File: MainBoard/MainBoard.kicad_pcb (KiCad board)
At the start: 2 copper layers, 31.8 x 110 mm, 41 parts, among them U1 TL074CN, U2 TL074CN, U3 TL074CN

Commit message: updated placement
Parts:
- D1: value 1N5934B -> 1N5394B; footprint 1N5934B:P2_DO-201 -> 1N5349B:P2_DO-201
- D2: value 1N5934B -> 1N5349B; footprint 1N5934B:P2_DO-201 -> 1N5349B:P2_DO-201
- moved C2 99.5 mm to (169.3, 144.5), turned to 90 degrees
- moved U1 95.0 mm to (155.3, 149.3)
- moved R3 91.5 mm to (150.5, 138.8)
- moved R1 90.5 mm to (150.5, 135.5), turned to 0 degrees
- moved C1 89.3 mm to (169.4, 152.7), turned to 90 degrees
- moved R9 89.1 mm to (139.6, 148.5), turned to 90 degrees
- moved D2 86.9 mm to (147.5, 49.6), turned to 0 degrees
- moved R2 86.5 mm to (143.3, 138.5), turned to -90 degrees
- moved R4 82.4 mm to (146.5, 125.7), turned to -90 degrees
- moved R16 81.6 mm to (160.6, 142.2), turned to 180 degrees
- moved R10 78.8 mm to (143.2, 135.8), turned to 90 degrees
- moved JP1 77.3 mm to (168.5, 70.9), turned to 90 degrees
- moved D1 77.1 mm to (147.5, 57.8), turned to 180 degrees
- moved F2 74.9 mm to (164.3, 50.5), turned to 0 degrees
- moved F1 73.7 mm to (159.3, 63.2), turned to -90 degrees
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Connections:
- Jheader2 pad 12: Output8 -> Output5
- Jheader2 pad 13: Output9 -> Output8
- Jheader2 pad 14: Output10 -> Output6
- Jheader2 pad 7: Output5 -> Output9
- Jheader2 pad 8: Output6 -> Output10
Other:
- board size 31.8 x 110 mm -> 34.4 x 110 mm

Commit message: first pass at routing mainboard
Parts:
- added R25: 100k, Resistor_THT:R_Axial_DIN0207_L6.3mm_D2.5mm_P10.16mm_Horizontal, F.Cu at (149.5, 141.5)
- Jheader2: footprint 61301611021:61301611021 -> 75168-116-20LF:AMPHENOL_75168-116-20LF
- moved F2 24.1 mm to (169.7, 74.0), turned to 90 degrees
- moved R16 23.2 mm to (146.2, 124.1), turned to 90 degrees
- moved C8 19.1 mm to (153.5, 55.3)
- moved R7 18.7 mm to (139.9, 54.4), turned to 0 degrees
- moved C2 18.3 mm to (151.0, 144.4), turned to -90 degrees
- moved R3 17.0 mm to (140.8, 152.8)
- moved R20 16.5 mm to (169.0, 118.0), turned to 90 degrees
- moved C7 11.2 mm to (165.7, 68.9)
- moved JP1 10.3 mm to (168.6, 60.6)
- moved F1 9.52 mm to (159.8, 53.7), turned to 90 degrees
- moved D1 8.07 mm to (152.8, 63.9)
- moved Jheader2 7.90 mm to (141.8, 91.5)
- moved C1 7.18 mm to (166.3, 146.2)
- moved R12 6.91 mm to (146.2, 100.7)
- moved C5 6.84 mm to (162.5, 85.1), turned to 180 degrees
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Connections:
- Jheader2 pad 10: InputBus4 -> Output10
- Jheader2 pad 11: Output7 -> InputBus4
- Jheader2 pad 12: Output5 -> Output4
- Jheader2 pad 13: Output8 -> Output9
- Jheader2 pad 14: Output6 -> Output12
- Jheader2 pad 15: Output11 -> Output3
- Jheader2 pad 16: Output12 -> Output11
- U1 pad 12: InputBus2 -> Net-(U1-4IN+)
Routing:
- net GND: track 0.00 -> 238.2 mm
- net -v: track 0.00 -> 144.6 mm
- net +v: track 0.00 -> 120.8 mm
- net InputBus2: track 0.00 -> 81.1 mm
- net InputBus3: track 0.00 -> 61.9 mm
- net Output3: track 0.00 -> 52.9 mm
- net Net-(U2-3IN-): track 0.00 -> 48.9 mm
- net Output4: track 0.00 -> 47.1 mm
- net Net-(U1-2IN-): track 0.00 -> 44.5 mm
- net InputBus4: track 0.00 -> 44.4 mm
- net Net-(U2-3IN+): track 0.00 -> 38.7 mm
- net Net-(U3-4IN-): track 0.00 -> 37.5 mm
- net Output2: track 0.00 -> 33.9 mm
- net InputBus1: track 0.00 -> 33.6 mm
- net Net-(U1-3IN-): track 0.00 -> 33.0 mm
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
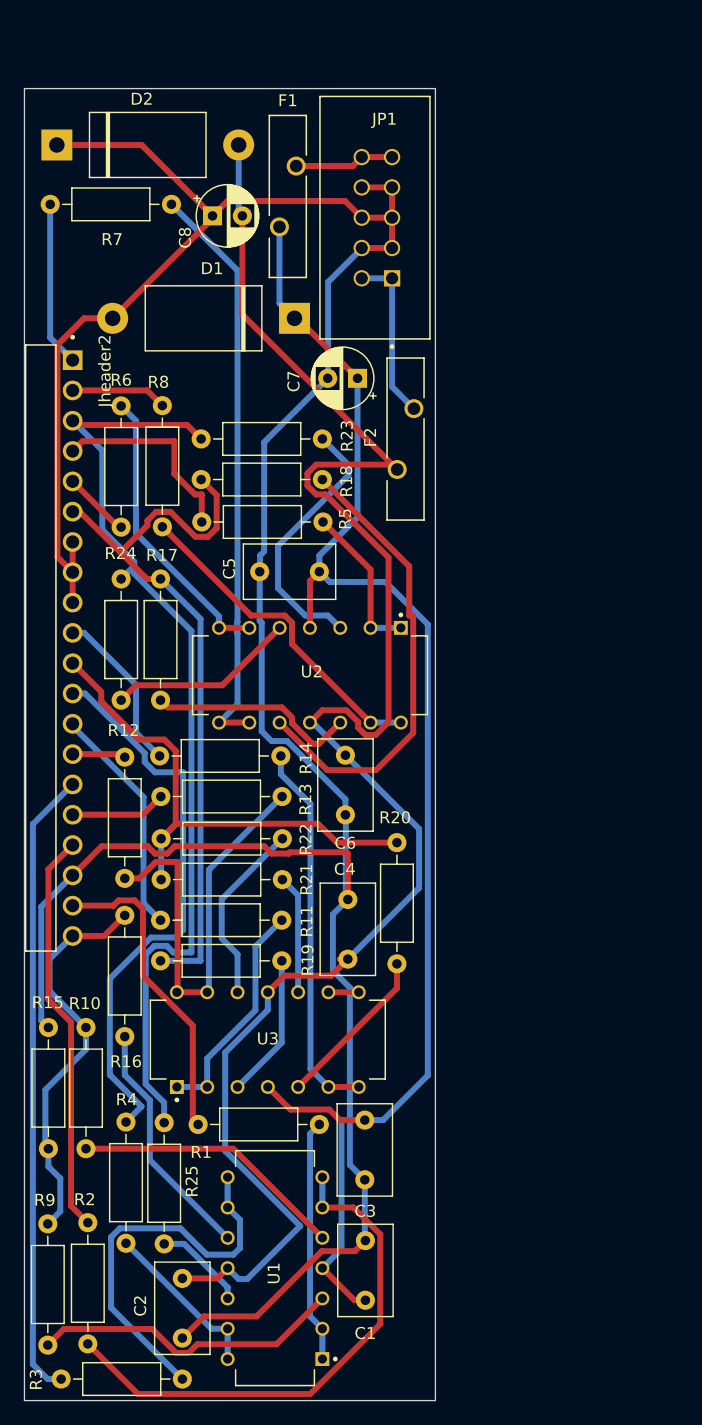
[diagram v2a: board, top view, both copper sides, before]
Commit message: added ground plane
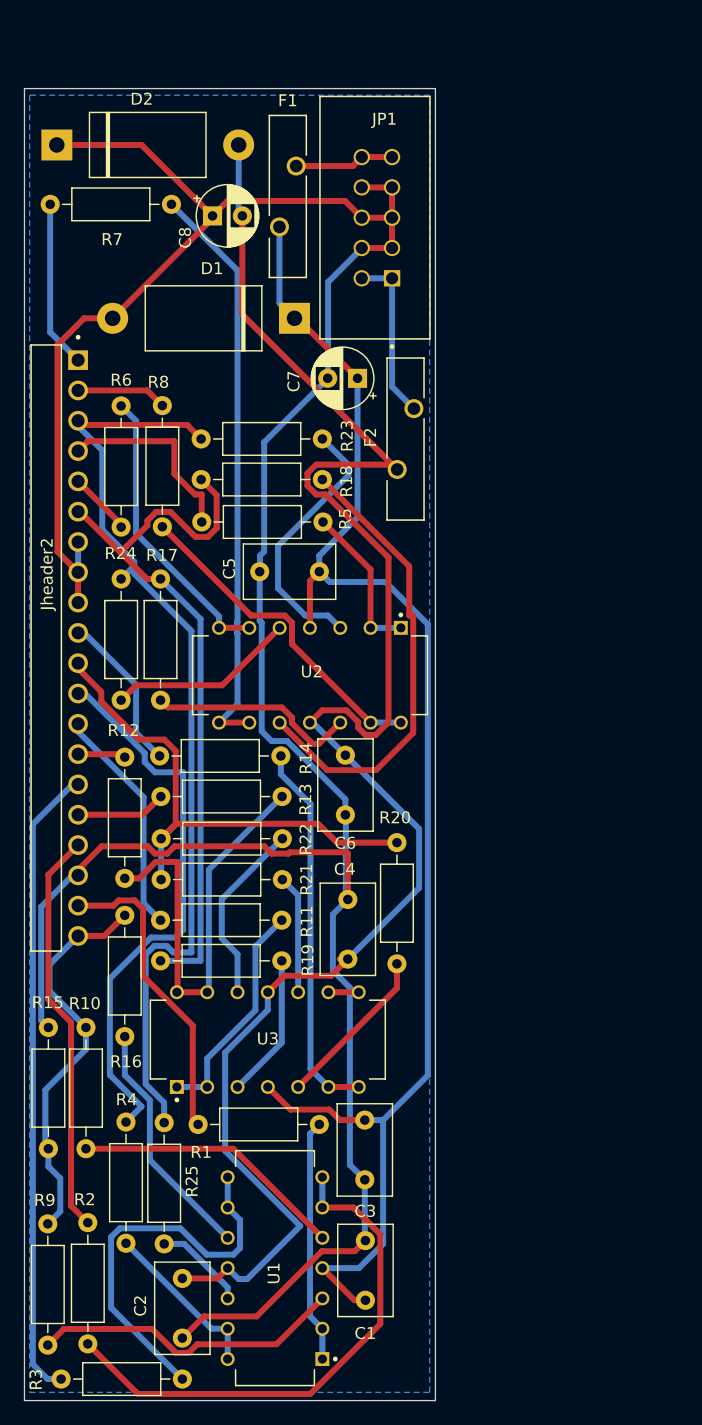
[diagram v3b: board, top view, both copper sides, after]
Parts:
- moved Jheader2 0.46 mm to (142.2, 91.5)
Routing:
- net +v: track 120.8 -> 124.0 mm
- net InputBus2: track 81.1 -> 79.5 mm
- net Output6: track 5.88 -> 5.33 mm
- net Output5: track 17.0 -> 16.5 mm
- added copper zone on B.Cu, net GND

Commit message: some updates
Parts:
- moved R10 0.15 mm to (143.1, 133.5)
- moved U2 0.06 mm to (161.6, 93.9)
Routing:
- net InputBus3: track 61.5 -> 67.4 mm
- net Output5: track 16.5 -> 13.3 mm
- net +v: track 124.0 -> 121.2 mm
- net Net-(U2-3IN+): track 38.7 -> 41.3 mm
- net -v: track 144.6 -> 142.0 mm
- net InputBus1: track 33.4 -> 31.5 mm
- net InputBus2: track 79.5 -> 77.9 mm
- net Net-(U1-2IN+): track 22.9 -> 24.5 mm
- net Net-(U1-4IN-): track 14.0 -> 15.4 mm
- net Net-(U2-2IN-): track 24.5 -> 25.9 mm
- net Net-(U1-3IN-): track 33.0 -> 34.3 mm
- net GND: track 238.4 -> 237.3 mm
- net Net-(U3-4IN+): track 15.5 -> 14.7 mm
- net Net-(U3-1IN-): track 19.1 -> 19.8 mm
- net Net-(U1-4IN+): track 7.76 -> 7.25 mm

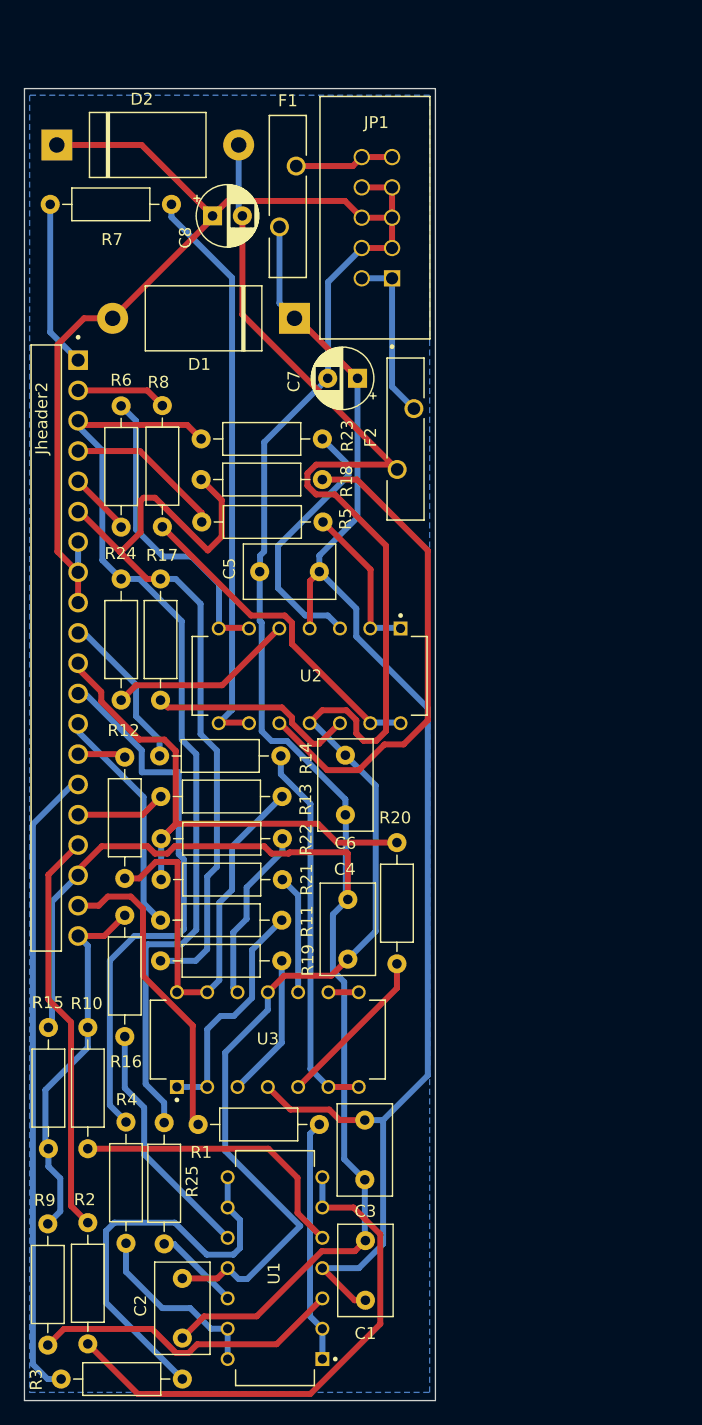
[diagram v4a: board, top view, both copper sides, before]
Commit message: removed ground loops
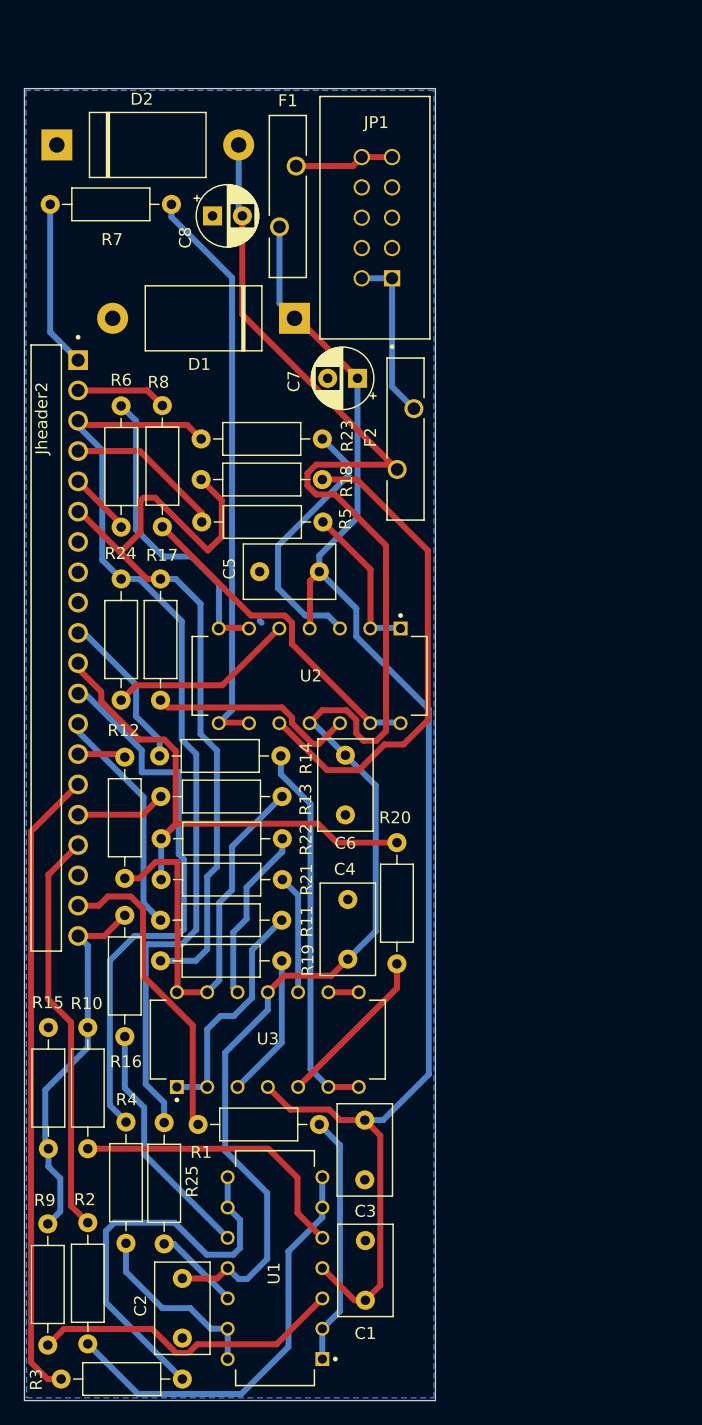
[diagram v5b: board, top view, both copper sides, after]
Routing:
- net GND: track 237.3 -> 0.67 mm
- net Net-(U1-2IN-): track 44.5 -> 35.6 mm
- net -v: track 142.0 -> 139.7 mm
- net Net-(U1-1IN-): track 20.4 -> 21.0 mm

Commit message: converted MainBoard to 4 layer stackup
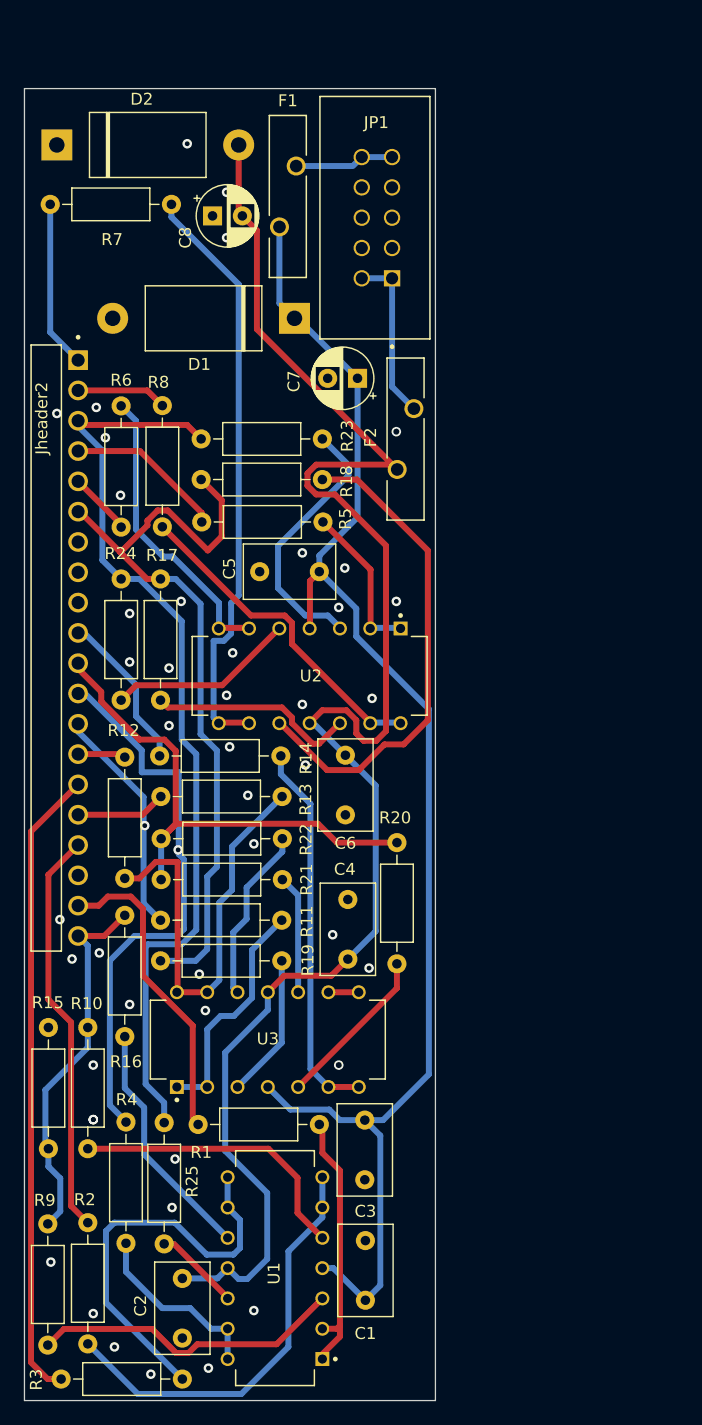
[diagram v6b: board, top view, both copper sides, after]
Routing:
- net InputBus3: track 67.4 -> 65.2 mm
- net Net-(U1-1IN-): track 21.0 -> 22.6 mm
- net Net-(U2-3IN-): track 48.6 -> 49.9 mm
- net Net-(U2-2IN-): track 25.9 -> 25.0 mm
- net GND: track 0.67 -> 0.00 mm, vias 0 -> 45
- net Output9: track 19.3 -> 19.4 mm, vias 0 -> 1
- net Output4: vias 0 -> 1
- added copper zone on In1.Cu, net GND
- added copper zone on In2.Cu, net GND
- removed copper zone on B.Cu, net GND
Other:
- copper layers 2 -> 4

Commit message: WIP: added faceplate
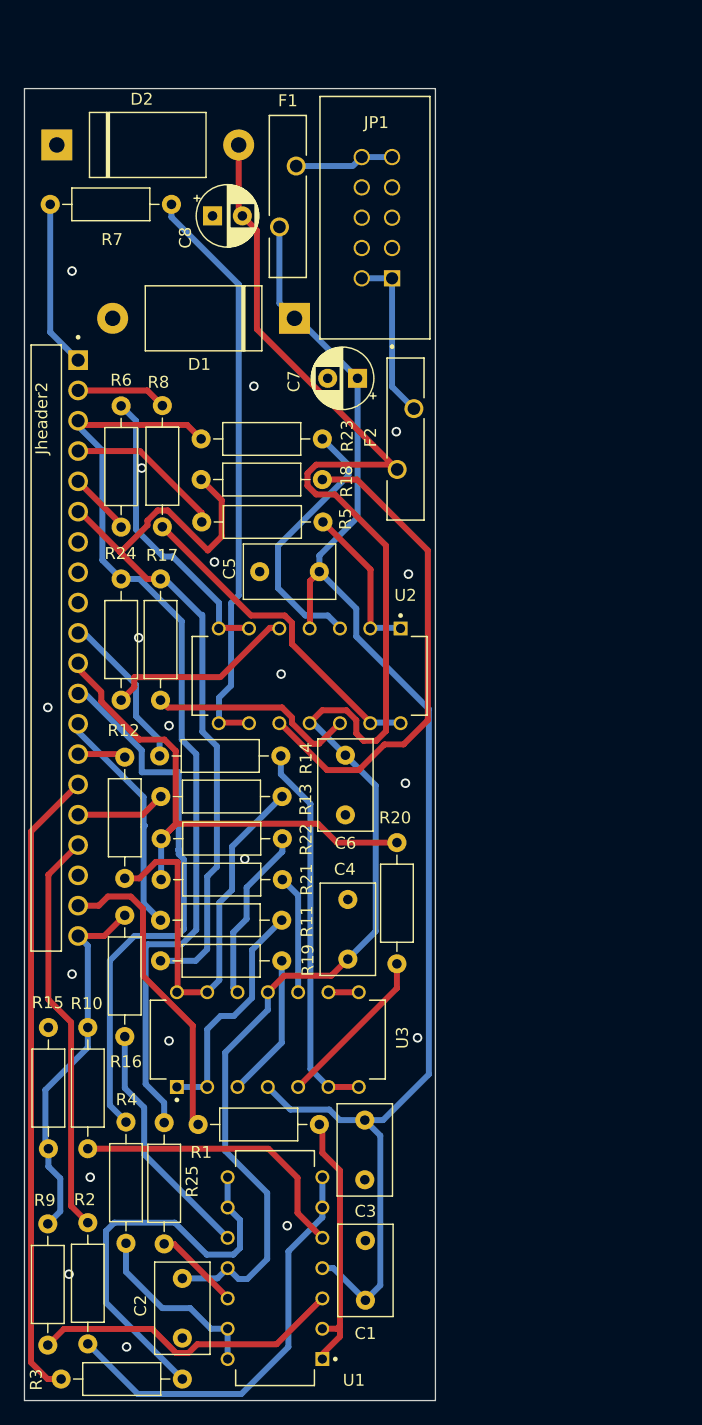
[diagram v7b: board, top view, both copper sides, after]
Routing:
- net Net-(U2-3IN-): track 49.9 -> 49.1 mm
- net InputBus3: track 65.2 -> 64.6 mm
- net Output9: vias 1 -> 0
- net Output4: vias 1 -> 0
- net GND: vias 45 -> 19

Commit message: sent to production v1.0.0
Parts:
- moved C1 20.9 mm to (186.6, 140.9)
- moved C2 20.9 mm to (171.2, 139.1)
- moved C5 20.9 mm to (182.7, 79.9)
- moved C6 20.9 mm to (184.9, 95.2)
- moved JP1 20.9 mm to (188.8, 55.3)
- moved Jheader2 20.9 mm to (162.5, 86.3)
- moved R1 20.9 mm to (172.6, 126.2)
- moved R10 20.9 mm to (163.3, 128.2)
- moved R11 20.9 mm to (169.4, 109.1)
- moved R14 20.9 mm to (169.3, 95.3)
- moved R15 20.9 mm to (160.0, 128.2)
- moved R16 20.9 mm to (166.4, 118.8)
- moved R18 20.9 mm to (183.0, 72.1)
- moved R19 20.9 mm to (179.6, 112.5)
- moved R23 20.9 mm to (172.8, 68.7)
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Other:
- board text added: "R-mods v1.0.0 2023"
